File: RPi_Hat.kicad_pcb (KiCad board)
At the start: 2 copper layers, 65 x 56.5 mm, 16 parts, among them IC1 0.96_I2C_OLED, IC4 0.96_I2C_OLED, J1 RPi_GPIO, J2 TCBM, SW1 Select, SW2 Up, SW3 Down, SW4 Exit, SW5 Add Disk

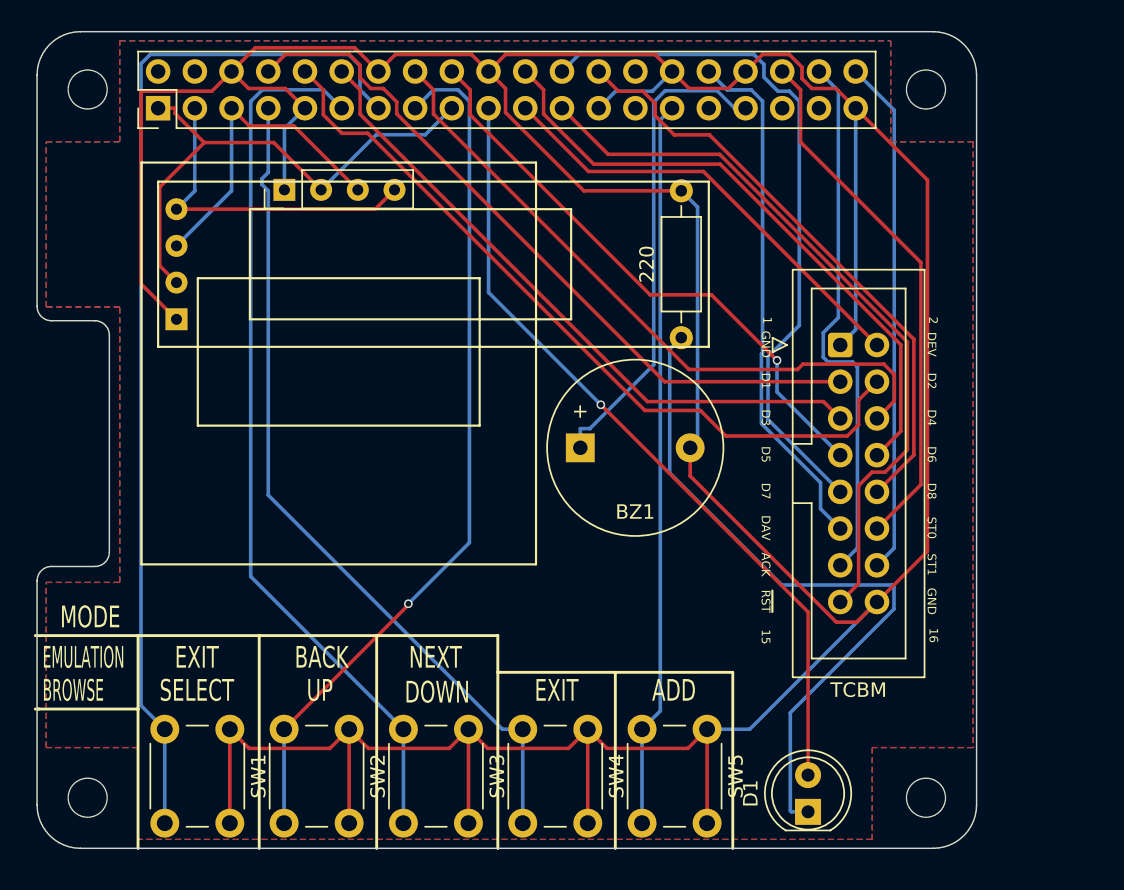
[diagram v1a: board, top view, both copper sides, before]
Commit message: completed tht version with tape interface support
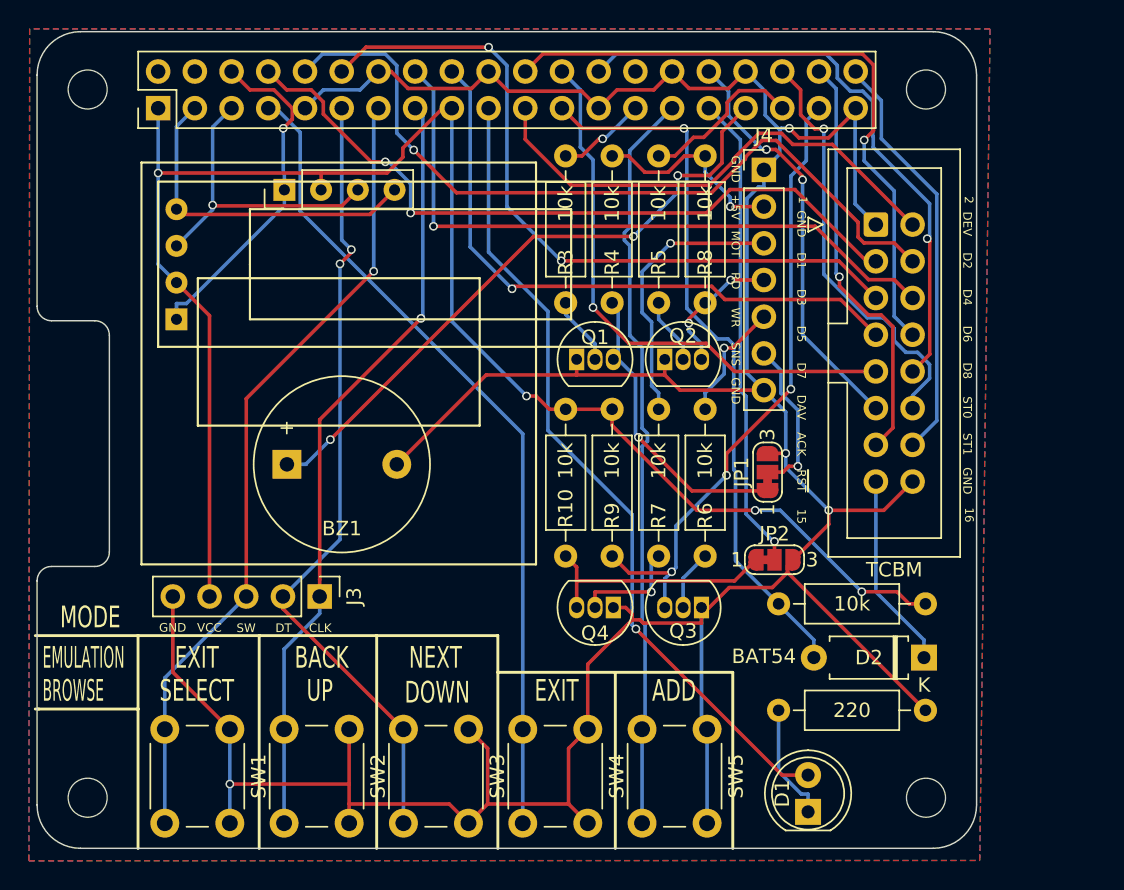
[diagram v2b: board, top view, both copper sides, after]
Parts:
- added D2: BAT54, Diode_THT:D_A-405_P7.62mm_Horizontal, F.Cu at (84.9, 71.9)
- added J3: Conn_01x05, Connector_PinHeader_2.54mm:PinHeader_1x05_P2.54mm_Vertical, F.Cu at (43.0, 67.7)
- added J4: Mini-DIN-7, Connector_PinHeader_2.54mm:PinHeader_1x07_P2.54mm_Vertical, F.Cu at (73.8, 38.1)
- added JP1: SolderJumper_3_Bridged12, Jumper:SolderJumper-3_P1.3mm_Bridged12_RoundedPad1.0x1.5mm_NumberLabels, F.Cu at (74.0, 59.0)
- added JP2: SolderJumper_3_Bridged12, Jumper:SolderJumper-3_P1.3mm_Bridged12_RoundedPad1.0x1.5mm_NumberLabels, F.Cu at (74.5, 65.1)
- added Q1: NPN: 2n3904, Package_TO_SOT_THT:TO-92_Inline, F.Cu at (60.8, 51.2)
- added Q2: NPN: 2n3904, Package_TO_SOT_THT:TO-92_Inline, F.Cu at (66.9, 51.2)
- added Q3: NPN: 2n3904, Package_TO_SOT_THT:TO-92_Inline, F.Cu at (69.5, 68.4)
- added Q4: NPN: 2n3904, Package_TO_SOT_THT:TO-92_Inline, F.Cu at (63.4, 68.4)
- added R10: 10k, Resistor_THT:R_Axial_DIN0207_L6.3mm_D2.5mm_P10.16mm_Horizontal, F.Cu at (60.1, 64.9)
- added R2: 10k, Resistor_THT:R_Axial_DIN0207_L6.3mm_D2.5mm_P10.16mm_Horizontal, F.Cu at (74.8, 68.2)
- added R3: 10k, Resistor_THT:R_Axial_DIN0207_L6.3mm_D2.5mm_P10.16mm_Horizontal, F.Cu at (60.1, 47.3)
- added R4: 10k, Resistor_THT:R_Axial_DIN0207_L6.3mm_D2.5mm_P10.16mm_Horizontal, F.Cu at (63.3, 47.3)
- added R5: 10k, Resistor_THT:R_Axial_DIN0207_L6.3mm_D2.5mm_P10.16mm_Horizontal, F.Cu at (66.5, 47.3)
- added R6: 10k, Resistor_THT:R_Axial_DIN0207_L6.3mm_D2.5mm_P10.16mm_Horizontal, F.Cu at (69.7, 64.9)
- added R7: 10k, Resistor_THT:R_Axial_DIN0207_L6.3mm_D2.5mm_P10.16mm_Horizontal, F.Cu at (66.5, 64.9)
- added R8: 10k, Resistor_THT:R_Axial_DIN0207_L6.3mm_D2.5mm_P10.16mm_Horizontal, F.Cu at (69.7, 47.3)
- added R9: 10k, Resistor_THT:R_Axial_DIN0207_L6.3mm_D2.5mm_P10.16mm_Horizontal, F.Cu at (63.3, 64.9)
- moved R1 39.7 mm to (85.0, 75.5), turned to 180 degrees
- moved BZ1 20.3 mm to (40.8, 58.5)
- moved J2 8.69 mm to (81.5, 41.9)
- renumbered IC4 to IC1, IC1 to IC2
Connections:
- J1 pad 23: /~{RESET} -> /~{RESET_3V3}
- J1 pad 27: unconnected-(J1-BCM0_ID_SD-Pad27) -> /TAP_SENSE
- J1 pad 31: unconnected-(J1-BCM6-Pad31) -> /TAP_MOTOR
- J1 pad 35: unconnected-(J1-BCM19_MISO-Pad35) -> /TAP_READ
- J1 pad 37: unconnected-(J1-BCM26-Pad37) -> /TAP_WRITE
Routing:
- net +3V3: track 36.7 -> 115.2 mm, vias 0 -> 4
- net /~{RESET_3V3}: track 0.00 -> 49.8 mm, vias 0 -> 1
- net /TAP_WRITE: track 0.00 -> 43.6 mm, vias 0 -> 3
- net Net-(D1-K): track 48.2 -> 8.14 mm
- net /~{RESET}: track 51.0 -> 13.6 mm
- net /TAP_MOTOR: track 0.00 -> 33.2 mm, vias 0 -> 1
- net Net-(JP1-A): track 0.00 -> 20.9 mm, vias 0 -> 1
- net GND: track 287.7 -> 268.2 mm, vias 0 -> 5
- net /CAS_MOTOR: track 0.00 -> 19.2 mm, vias 0 -> 1
- net Net-(JP2-A): track 0.00 -> 16.9 mm
- net /IN_SW1: track 72.4 -> 55.6 mm, vias 0 -> 1
- net /VCC_5V: track 0.00 -> 13.9 mm, vias 0 -> 1
- net /TAP_READ: track 0.00 -> 11.4 mm
- net /CAS_SENSE: track 0.00 -> 11.0 mm, vias 0 -> 1
- net /RPI_SND: track 33.6 -> 43.9 mm, vias 0 -> 3
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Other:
- board text added: "+5V"
- board text added: "CLK"
- board text added: "DT"
- board text added: "MOT"
- board text added: "Maciej Witkowiak <ytm@elysium.pl>, XII 2025"
- board text added: "RD"
- board text added: "SNS"
- board text added: "SW"
- board text added: "VCC"
- board text added: "WR"
- board text removed: "Maciej Witkowiak <ytm@elysium.pl>, X 2025"
- board text removed: "https://cbm-pi1541.firebaseapp.com"

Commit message: SMD rework and updates
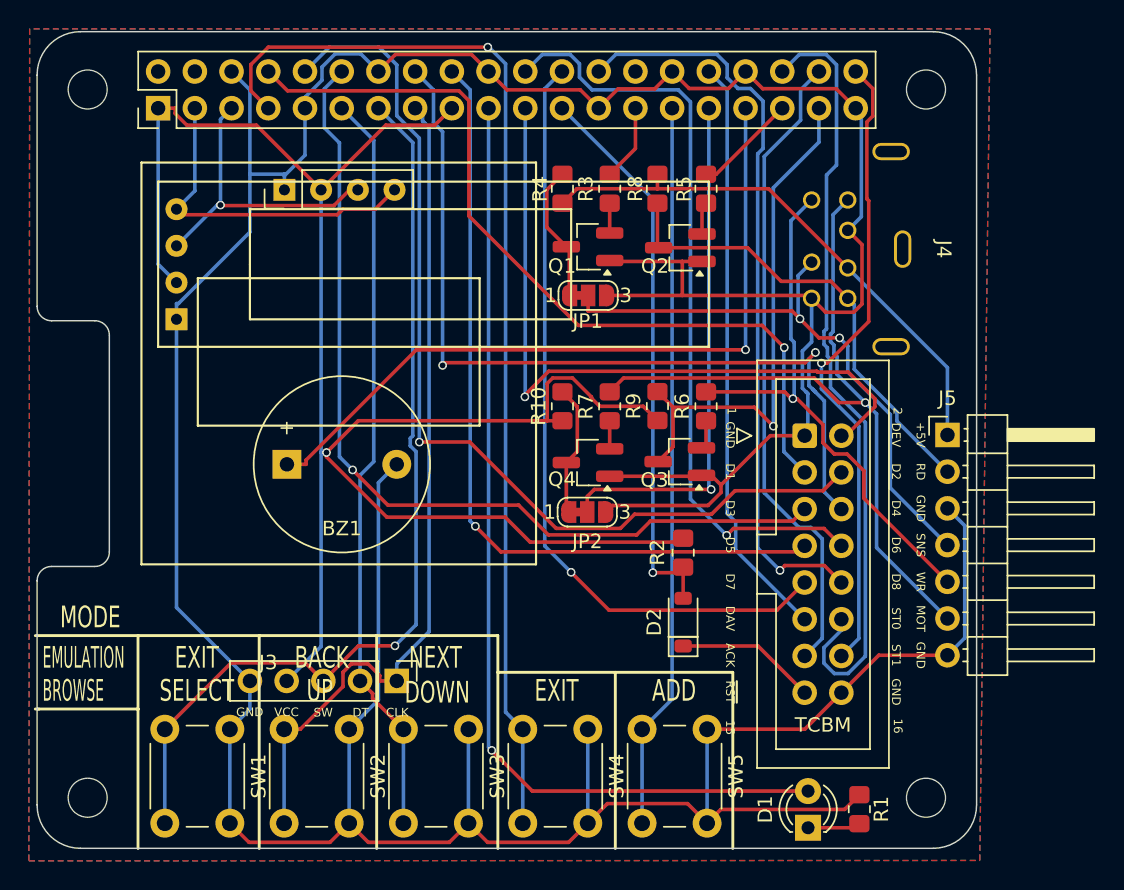
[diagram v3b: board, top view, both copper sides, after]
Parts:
- added J5: Conn_01x07, Connector_PinHeader_2.54mm:PinHeader_1x07_P2.54mm_Horizontal, F.Cu at (86.5, 56.5)
- D1: footprint LED_THT:LED_D5.0mm -> LED_THT:LED_D3.0mm
- D2: footprint Diode_THT:D_A-405_P7.62mm_Horizontal -> Diode_SMD:D_SOD-123
- J4: footprint Connector_PinHeader_2.54mm:PinHeader_1x07_P2.54mm_Vertical -> Conn_DIN_round:Mini_DIN_round_7_canned
- Q1, Q2, Q3, Q4: footprint Package_TO_SOT_THT:TO-92_Inline -> Package_TO_SOT_SMD:SOT-23_Handsoldering
- R1, R10, R2, R3, R4, R5, R6, R7, R8, R9: footprint Resistor_THT:R_Axial_DIN0207_L6.3mm_D2.5mm_P10.16mm_Horizontal -> Resistor_SMD:R_0805_2012Metric_Pad1.20x1.40mm_HandSolder
- moved JP1 17.4 mm to (61.6, 46.8), turned to 0 degrees
- moved D2 16.8 mm to (68.2, 69.4), turned to 90 degrees
- moved J2 15.4 mm to (76.6, 56.5)
- moved J4 15.3 mm to (88.1, 43.6), turned to -90 degrees
- moved JP2 13.4 mm to (61.6, 61.8)
- moved R7 10.9 mm to (63.1, 54.5)
- moved R9 10.8 mm to (66.4, 54.5)
- moved R10 10.4 mm to (59.8, 54.5)
- moved R6 10.4 mm to (69.8, 54.5)
- moved Q3 10.2 mm to (68.0, 58.3)
- moved Q4 10.2 mm to (61.6, 58.4)
- moved R4 8.61 mm to (59.8, 39.4)
- moved R8 8.55 mm to (66.4, 39.4), turned to -90 degrees
- moved R5 8.54 mm to (69.8, 39.4)
- moved R3 8.46 mm to (63.1, 39.4)
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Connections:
- R1 pad 1: GND -> Net-(D1-K)
- R1 pad 2: Net-(D1-K) -> GND
- R10 pad 1: Net-(JP2-A) -> +3V3
- R10 pad 2: +3V3 -> Net-(JP2-A)
- R2 pad 1: /~{RESET_3V3} -> +3V3
- R2 pad 2: +3V3 -> /~{RESET_3V3}
- R4 pad 1: Net-(JP1-A) -> /VCC_5V
- R4 pad 2: /VCC_5V -> Net-(JP1-A)
- R8 pad 1: /CAS_READ -> /VCC_5V
- R8 pad 2: /VCC_5V -> /CAS_READ
- R9 pad 1: /TAP_WRITE -> +3V3
- R9 pad 2: +3V3 -> /TAP_WRITE
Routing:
- net GND: track 268.2 -> 312.8 mm, vias 5 -> 0
- net /CAS_MOTOR: track 19.2 -> 51.6 mm
- net /CAS_WRITE: track 8.43 -> 39.3 mm
- net /CAS_SENSE: track 11.0 -> 41.0 mm, vias 1 -> 2
- net /STATUS0: track 29.5 -> 54.2 mm, vias 1 -> 0
- net /VCC_5V: track 13.9 -> 37.8 mm, vias 1 -> 0
- net /CAS_READ: track 9.47 -> 32.5 mm, vias 2 -> 0
- net /IN_SW4: track 57.1 -> 75.1 mm, vias 0 -> 1
- net /ACK: track 29.0 -> 44.7 mm, vias 1 -> 0
- net /STATUS1: track 28.8 -> 44.3 mm, vias 0 -> 1
- net /DIO7: track 38.6 -> 53.9 mm
- net /DEV: track 34.5 -> 49.5 mm, vias 0 -> 1
- net +3V3: track 115.2 -> 129.5 mm, vias 4 -> 1
- net /DIO4: track 46.4 -> 59.5 mm, vias 1 -> 2
- net /DIO2: track 54.9 -> 67.6 mm
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
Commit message: final version for test fabrication, added encoder part directly (without module, without pullups)
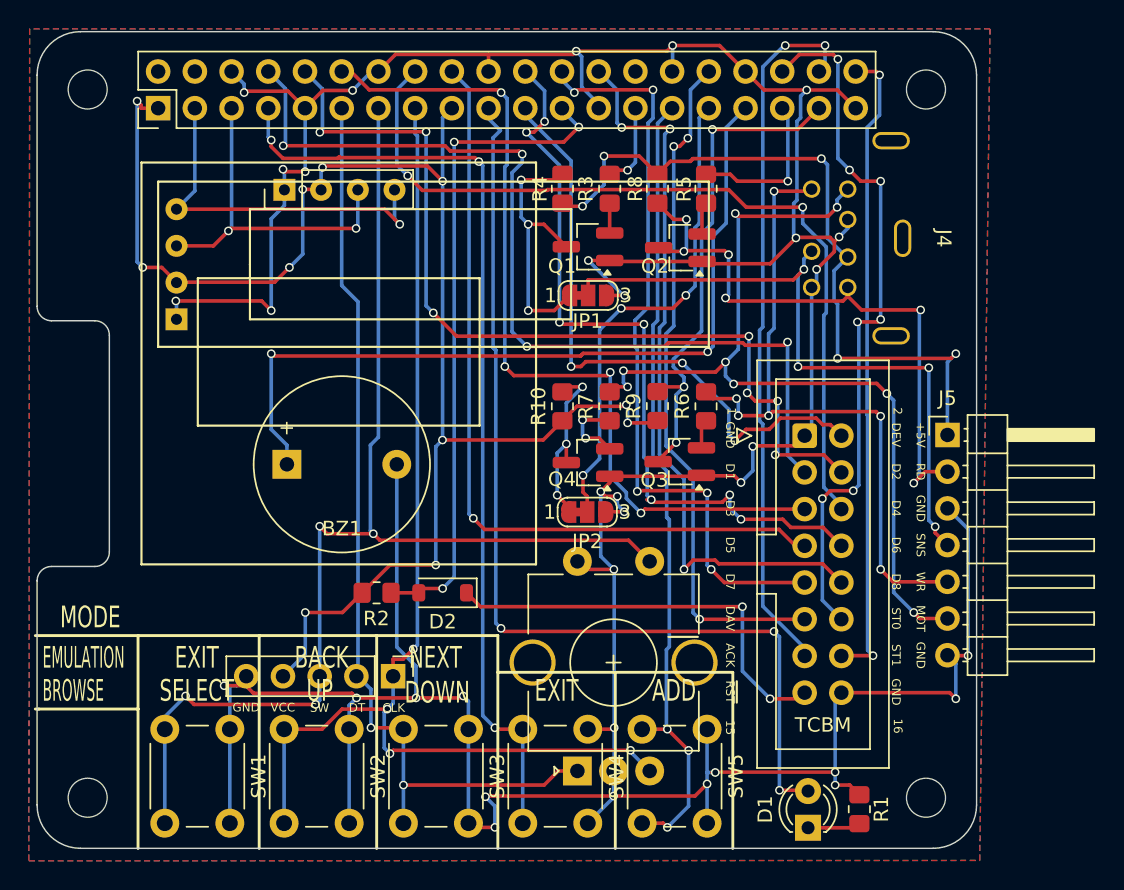
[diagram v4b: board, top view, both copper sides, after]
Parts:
- added SW6: RotaryEncoder_Switch, Rotary_Encoder:RotaryEncoder_Alps_EC11E-Switch_Vertical_H20mm_CircularMountingHoles, F.Cu at (60.9, 79.7)
- moved R2 21.4 mm to (47.0, 67.4), turned to 0 degrees
- moved D2 16.8 mm to (51.6, 67.4), turned to 180 degrees
- moved J4 0.75 mm to (88.1, 42.9)
- moved J3 0.41 mm to (48.1, 73.2)
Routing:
- net +3V3: track 129.5 -> 106.6 mm, vias 1 -> 11
- net /IN_SW2: track 58.7 -> 79.2 mm, vias 0 -> 4
- net /IN_SW1: track 64.9 -> 84.7 mm, vias 1 -> 4
- net /~{RESET}: track 9.74 -> 29.2 mm, vias 0 -> 2
- net /VCC_5V: track 37.8 -> 51.1 mm, vias 0 -> 5
- net /IN_SW3: track 52.0 -> 65.0 mm, vias 0 -> 2
- net /CAS_READ: track 32.5 -> 42.5 mm, vias 0 -> 6
- net Net-(JP1-A): track 9.47 -> 18.8 mm, vias 0 -> 3
- net /IN_SW4: track 75.1 -> 65.9 mm, vias 1 -> 3
- net /CAS_MOTOR: track 51.6 -> 60.8 mm, vias 1 -> 8
- net /CAS_WRITE: track 39.3 -> 47.6 mm, vias 1 -> 6
- net /DEV: track 49.5 -> 42.5 mm, vias 1 -> 3
- net /DAV: track 40.6 -> 47.6 mm, vias 0 -> 3
- net /~{RESET_3V3}: track 39.2 -> 45.8 mm, vias 1 -> 3
- net /DIO1: track 58.1 -> 64.5 mm, vias 1 -> 4
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
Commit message: - correct part and pinout for SMD 2n3904 transistor - added jumpers to configure VCC/GND routing for OLED screens - moved encoder to the left, module socket to the right
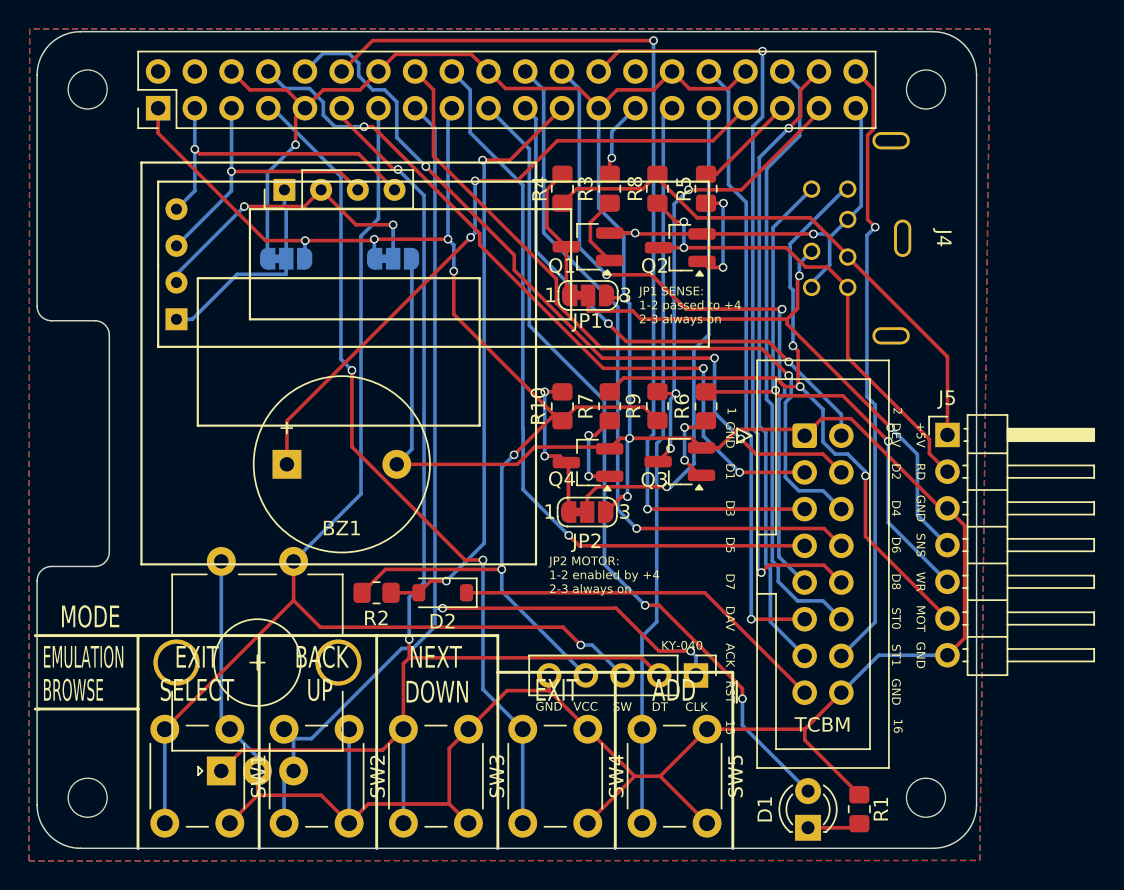
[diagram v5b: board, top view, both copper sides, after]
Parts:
- added JP3: SolderJumper_3_Bridged12, Jumper:SolderJumper-3_P1.3mm_Bridged12_RoundedPad1.0x1.5mm_NumberLabels, B.Cu at (40.7, 44.3)
- added JP4: SolderJumper_3_Bridged12, Jumper:SolderJumper-3_P1.3mm_Bridged12_RoundedPad1.0x1.5mm_NumberLabels, B.Cu at (48.1, 44.3)
- Q1, Q2, Q3, Q4: value NPN: 2n3904 -> MMBT3904
- moved SW6 24.6 mm to (36.2, 79.7)
- moved J3 21.0 mm to (69.1, 73.1)
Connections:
- IC1 pad 1: GND -> Net-(IC1-GND)
- IC1 pad 2: +3V3 -> Net-(IC1-VCC)
- IC2 pad 1: GND -> Net-(IC1-GND)
- IC2 pad 2: +3V3 -> Net-(IC1-VCC)
- Q1 pad 1: GND -> Net-(Q1-B)
- Q1 pad 2: Net-(Q1-B) -> GND
- Q2 pad 1: GND -> Net-(Q2-B)
- Q2 pad 2: Net-(Q2-B) -> GND
- Q3 pad 1: GND -> Net-(Q3-B)
- Q3 pad 2: Net-(Q3-B) -> GND
- Q4 pad 1: GND -> Net-(Q4-B)
- Q4 pad 2: Net-(Q4-B) -> GND
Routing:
- net GND: track 310.9 -> 288.3 mm, vias 34 -> 6
- net Net-(IC1-VCC): track 0.00 -> 21.3 mm, vias 0 -> 2
- net /IN_SW3: track 65.0 -> 84.2 mm
- net Net-(IC1-GND): track 0.00 -> 14.8 mm
- net +3V3: track 106.6 -> 92.2 mm, vias 11 -> 6
- net /VCC_5V: track 51.1 -> 38.3 mm, vias 5 -> 0
- net /RPI_LED: track 69.2 -> 57.0 mm, vias 3 -> 2
- net /DIO1: track 64.5 -> 52.3 mm, vias 4 -> 3
- net /RPI_SND: track 56.5 -> 45.8 mm
- net /CAS_MOTOR: track 60.8 -> 50.3 mm, vias 8 -> 3
- net Net-(JP1-A): track 18.8 -> 9.47 mm, vias 3 -> 0
- net /DIO2: track 63.3 -> 54.4 mm, vias 7 -> 3
- net /CAS_READ: track 42.5 -> 34.0 mm, vias 6 -> 2
- net /IN_SW4: track 65.9 -> 57.7 mm, vias 3 -> 2
- net /DIO4: track 58.5 -> 50.3 mm, vias 2 -> 1
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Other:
- board text added: "GND|PIN2|VCC"
- board text added: "JP1 SENSE: 1-2 passed to +4 2-3 always on"
- board text added: "JP2 MOTOR: 1-2 enabled by +4 2-3 always on"
- board text added: "KY-040"
- board text added: "Maciej Witkowiak <ytm@elysium.pl>, II 2026"
- board text added: "OLED POWER PINOUT"
- board text added: "SDA|SCL|(PIN2)|(PIN1)"
- board text added: "VCC|PIN1|GND"
- board text removed: "Maciej Witkowiak <ytm@elysium.pl>, XII 2025"
